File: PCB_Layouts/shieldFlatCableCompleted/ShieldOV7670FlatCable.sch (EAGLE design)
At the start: 14 parts, among them X1 332-20

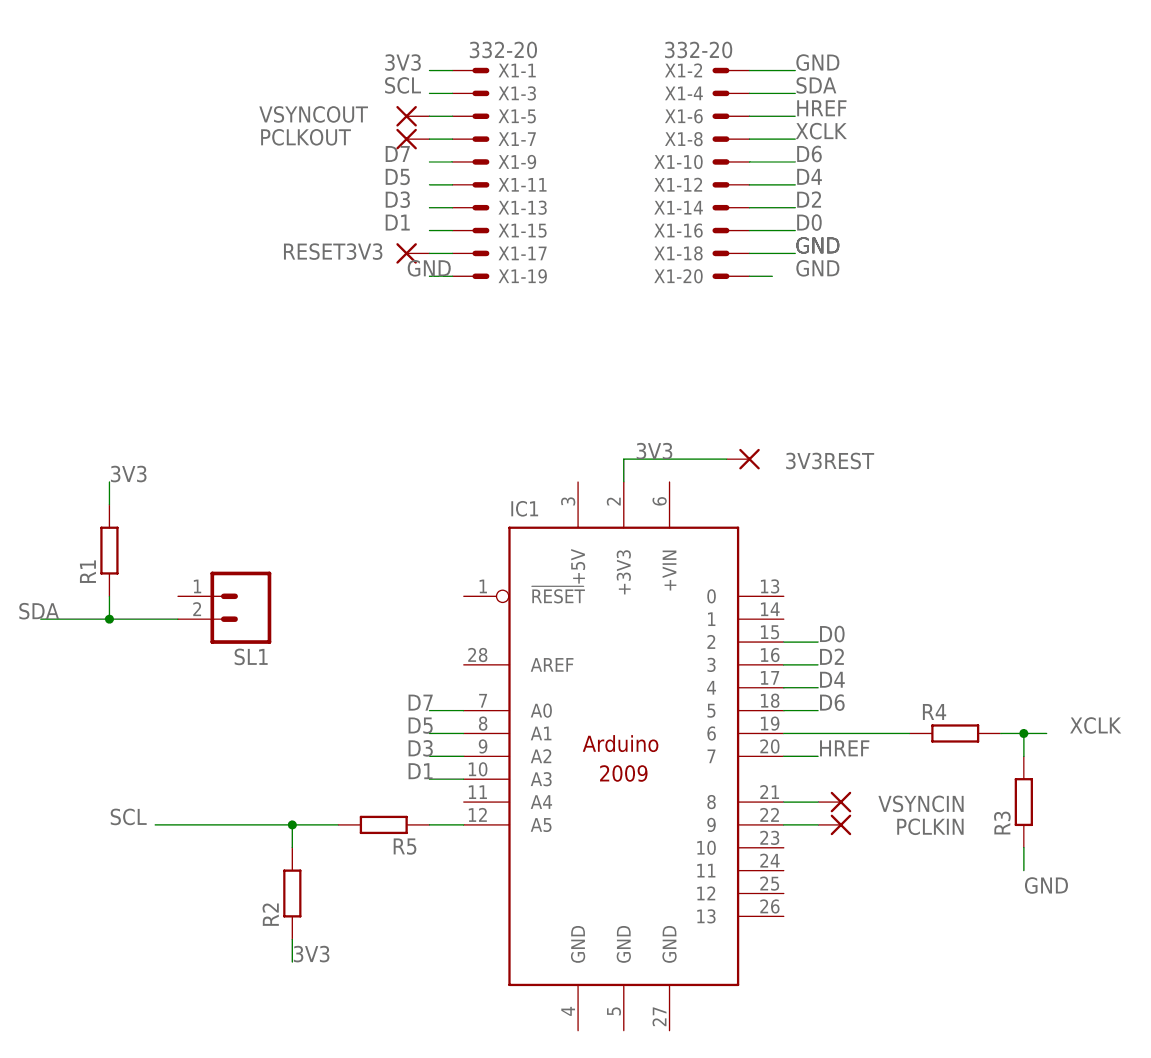
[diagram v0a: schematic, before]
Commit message: Add layout folder w/ flatcable adapter shield for arduino uno
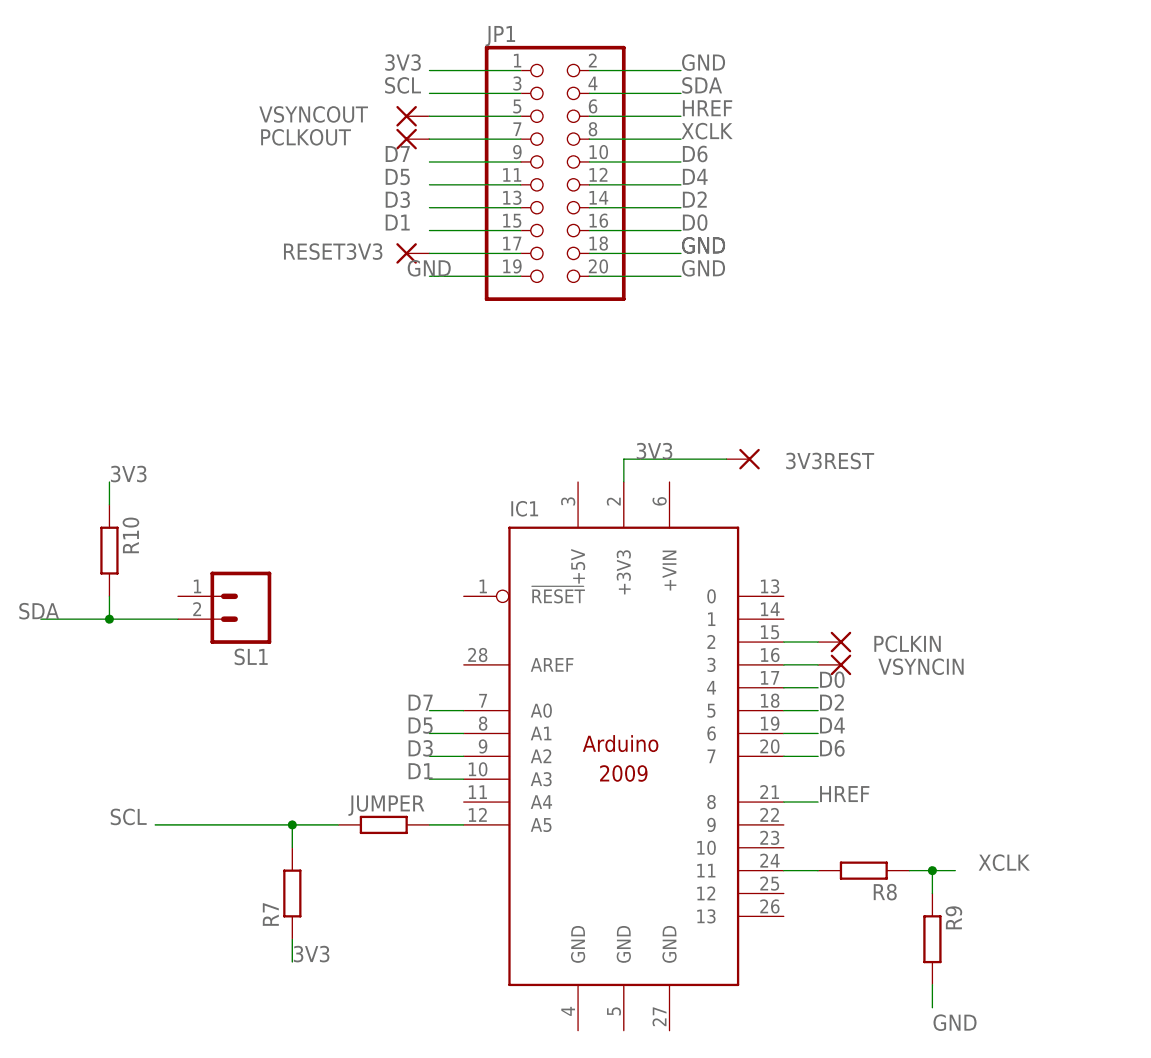
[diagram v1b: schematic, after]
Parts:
- removed R1, R2, R3, R4, R5: (no value), rcl:R-EU_0207/10
- removed X1: 332-20, con-garry:332-20
- added JP1: (no value), pinhead:PINHD-2X10
- added JUMPER, R10, R7, R8, R9: (no value), rcl:R-EU_0207/12
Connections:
- removed net N$9: IC1.6, R4.1
- new net N$7: IC1.11, R8.2
- net 3V3: now also JP1.1, R10.1, R7.1; no longer R1.2, R2.1, X1-1.S
- net D0: now also IC1.4, JP1.16; no longer IC1.2, X1-16.S
- net D1: now also JP1.15; no longer X1-15.S
- net D2: now also IC1.5, JP1.14; no longer IC1.3, X1-14.S
- net D3: now also JP1.13; no longer X1-13.S
- net D4: now also IC1.6, JP1.12; no longer IC1.4, X1-12.S
- net D5: now also JP1.11; no longer X1-11.S
- net D6: now also IC1.7, JP1.10; no longer IC1.5, X1-10.S
- net D7: now also JP1.9; no longer X1-9.S
- net GND: now also JP1.18, JP1.19, JP1.2, JP1.20, R9.2; no longer R3.1, X1-18.S, X1-19.S, X1-2.S, X1-20.S
- net HREF: now also IC1.8, JP1.6; no longer IC1.7, X1-6.S
- net N$1: now also IC1.2, PCLKIN.P; no longer IC1.8, VSYNCIN.P
- net N$2: now also IC1.3, VSYNCIN.P; no longer IC1.9, PCLKIN.P
- net N$3: now also JP1.5; no longer X1-5.S
- net N$4: now also JP1.7; no longer X1-7.S
- net N$5: now also JUMPER.2; no longer R5.1
- net N$6: now also JP1.17; no longer X1-17.S
- net SCL: now also JP1.3, JUMPER.1, R7.2; no longer R2.2, R5.2, X1-3.S
- net SDA: now also JP1.4, R10.2; no longer R1.1, X1-4.S
- net XCLK: now also JP1.8, R8.1, R9.1; no longer R3.2, R4.2, X1-8.S
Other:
- moved on the sheet: PCLKIN, VSYNCIN
